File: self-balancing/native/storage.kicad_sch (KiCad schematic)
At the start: 9 parts, among them U11 W25N01GVZEIG / 128MiB

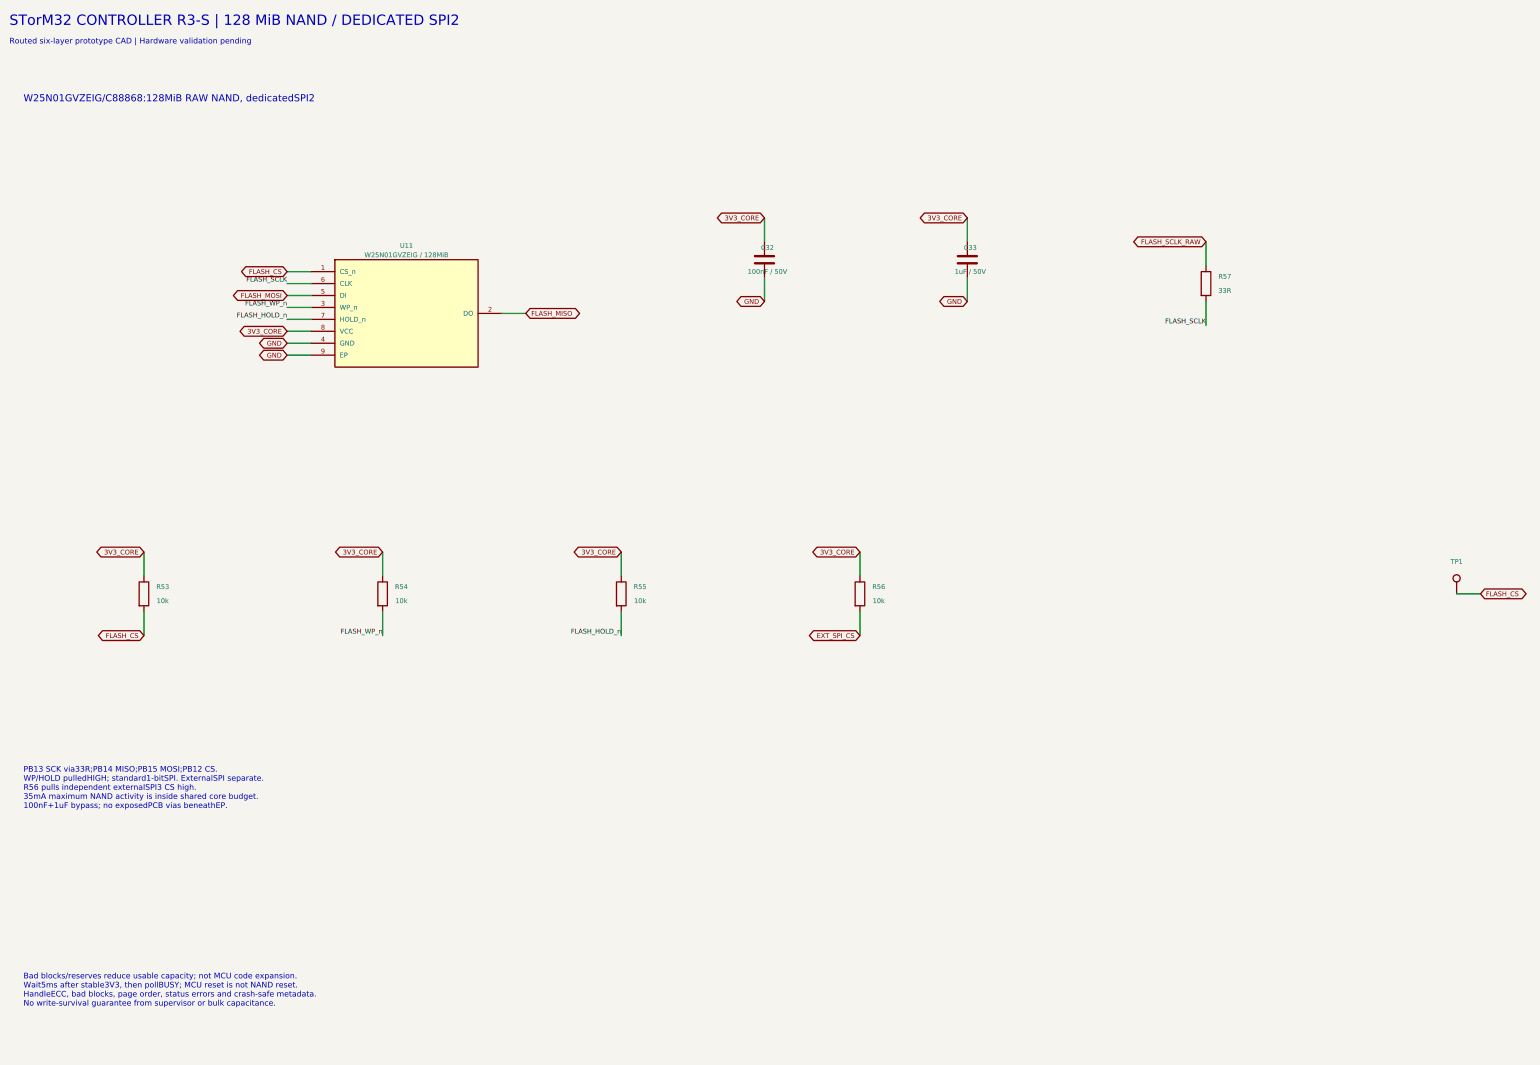
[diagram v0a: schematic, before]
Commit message: Improve H743 schematic readability with wired functional groups
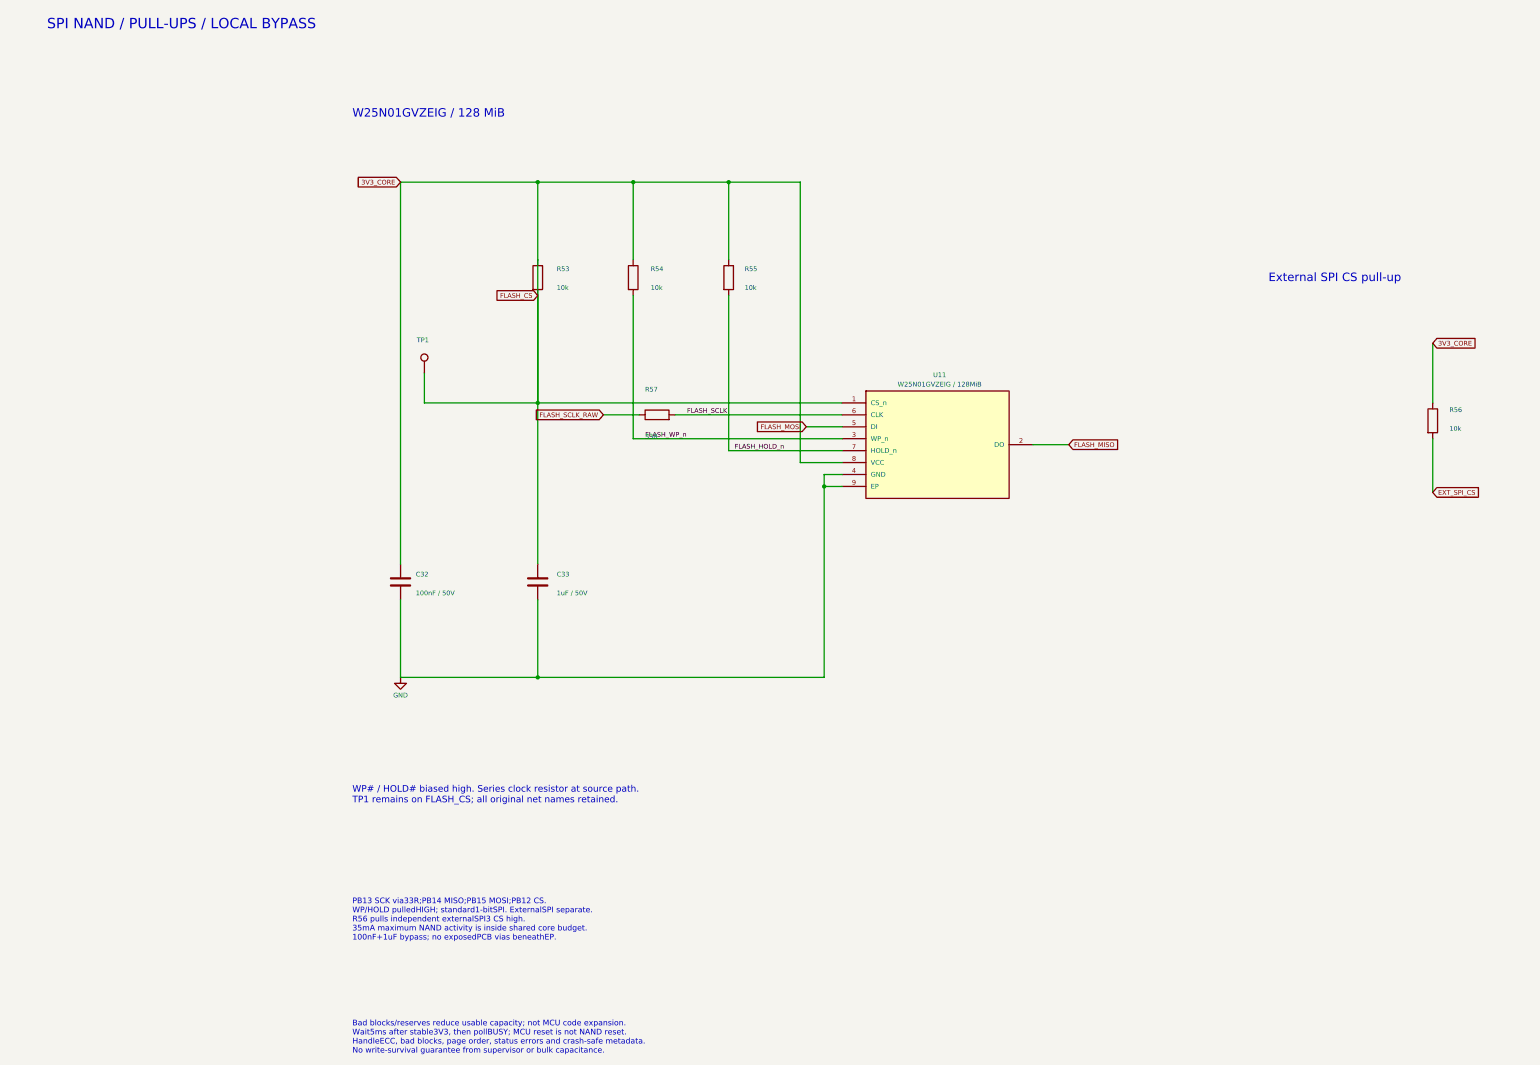
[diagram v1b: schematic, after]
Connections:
- net FLASH_CS is gone; now on net 3V3_CORE: R53.2, TP1.1, U11.1 (CS_n)
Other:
- note added: "External SPI CS pull-up"
- note added: "SPI NAND / PULL-UPS / LOCAL BYPASS"
- note added: "W25N01GVZEIG / 128 MiB"
- note added: "WP# / HOLD# biased high. Series clock resistor at source path. TP1 remains on FLASH_CS; all original net names retained."
- note removed: "Routed six-layer prototype CAD | Hardware validation pending"
- note removed: "STorM32 CONTROLLER R3-S | 128 MiB NAND / DEDICATED SPI2"
- note removed: "W25N01GVZEIG/C88868:128MiB RAW NAND, dedicatedSPI2"
- moved on the sheet: C32, C33, R53, R54, R55, R56, R57, TP1, U11

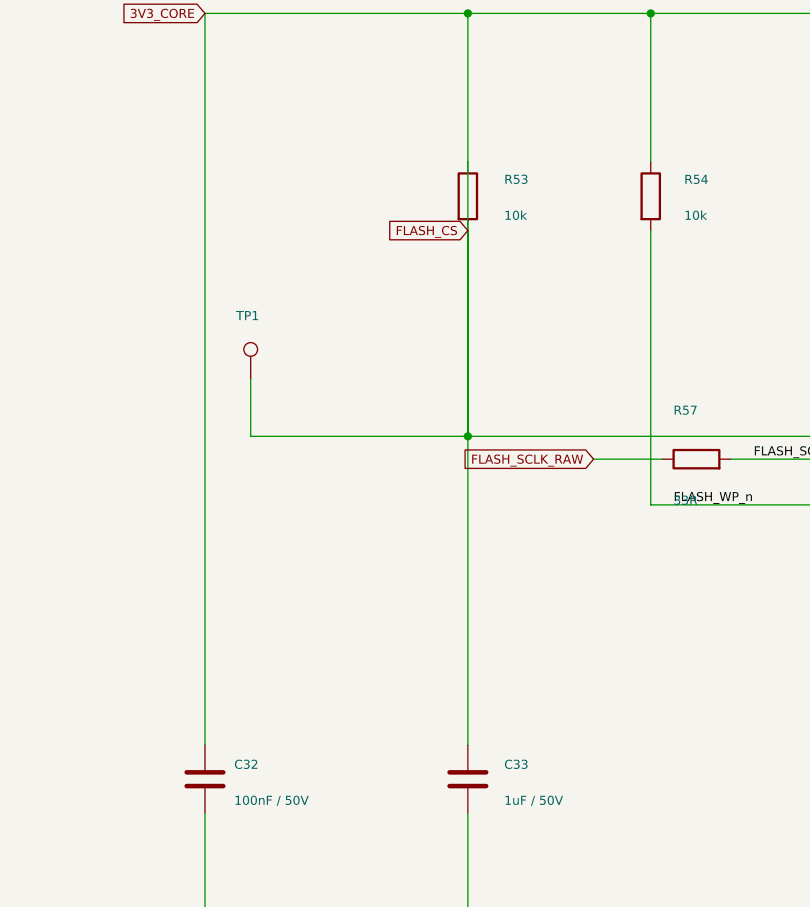
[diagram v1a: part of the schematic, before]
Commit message: Fix C33 supply wire crossing FLASH_CS pull-up
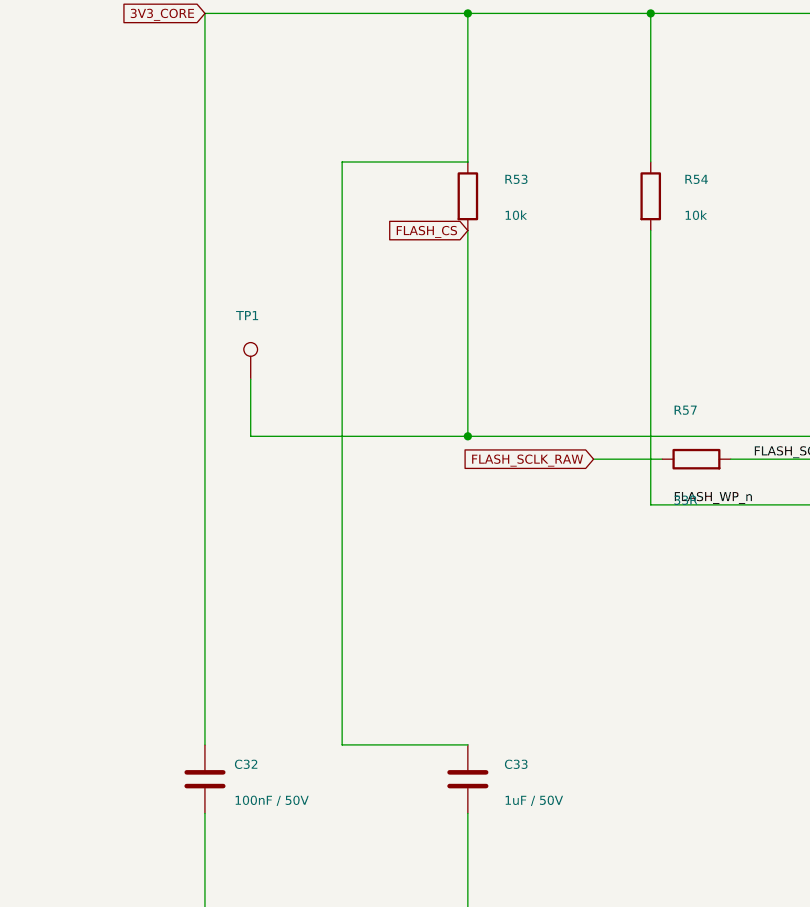
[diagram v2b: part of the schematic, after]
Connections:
- net 3V3_CORE: no longer R53.2, TP1.1, U11.1 (CS_n)
- new net FLASH_CS: R53.2, TP1.1, U11.1 (CS_n)
